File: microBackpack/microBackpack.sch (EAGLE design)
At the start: 71 parts, among them IC1 LM324D, IC2 LM324D, J2 USB_B_PTH, J4 2X6 FEMALE, U1 ATMEGA328P_TQFP, U2 5VREG-HS, U3 CP2102N-QFN24, U4 TVS_DIODE_4PK, U5 MCP4728, U6 78L09F, U7 TVS_DIODE_4PK, U8 TVS_DIODE_4PK, U9 TVS_DIODE_4PK

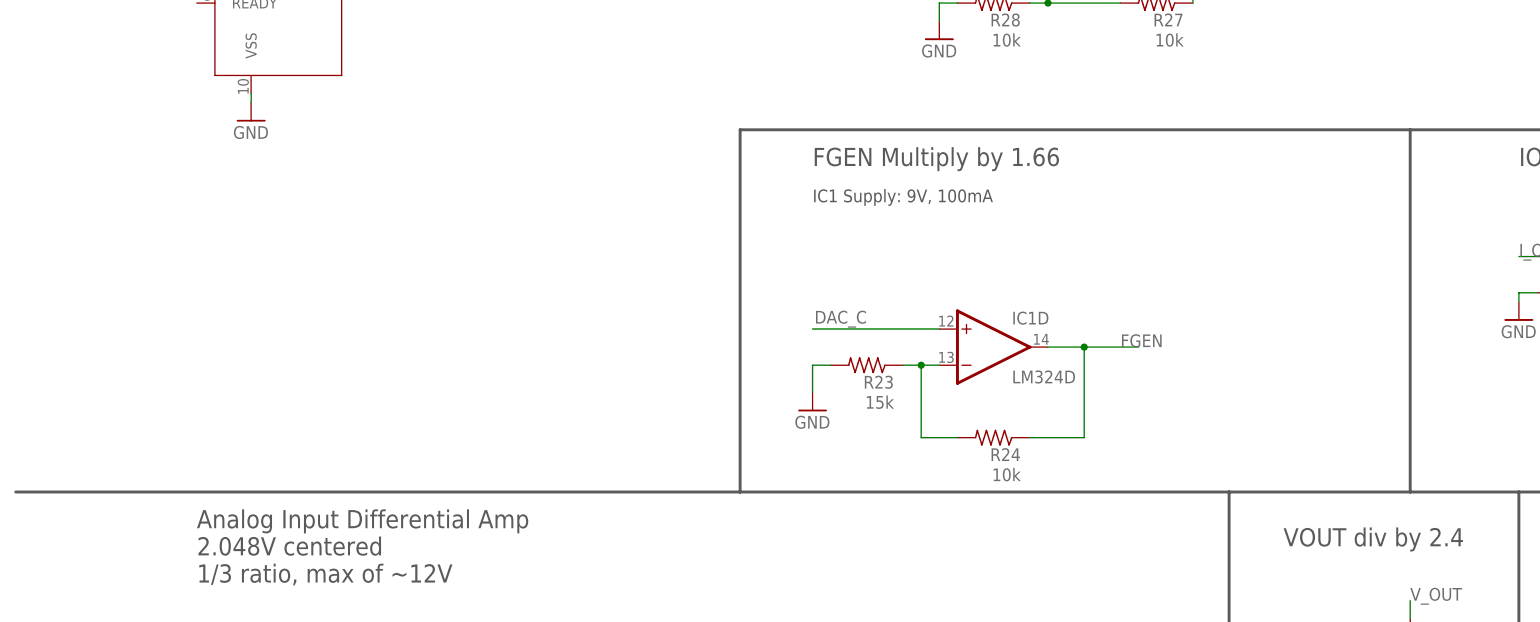
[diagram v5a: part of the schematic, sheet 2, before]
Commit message: Added 2nd order filter to FGEN
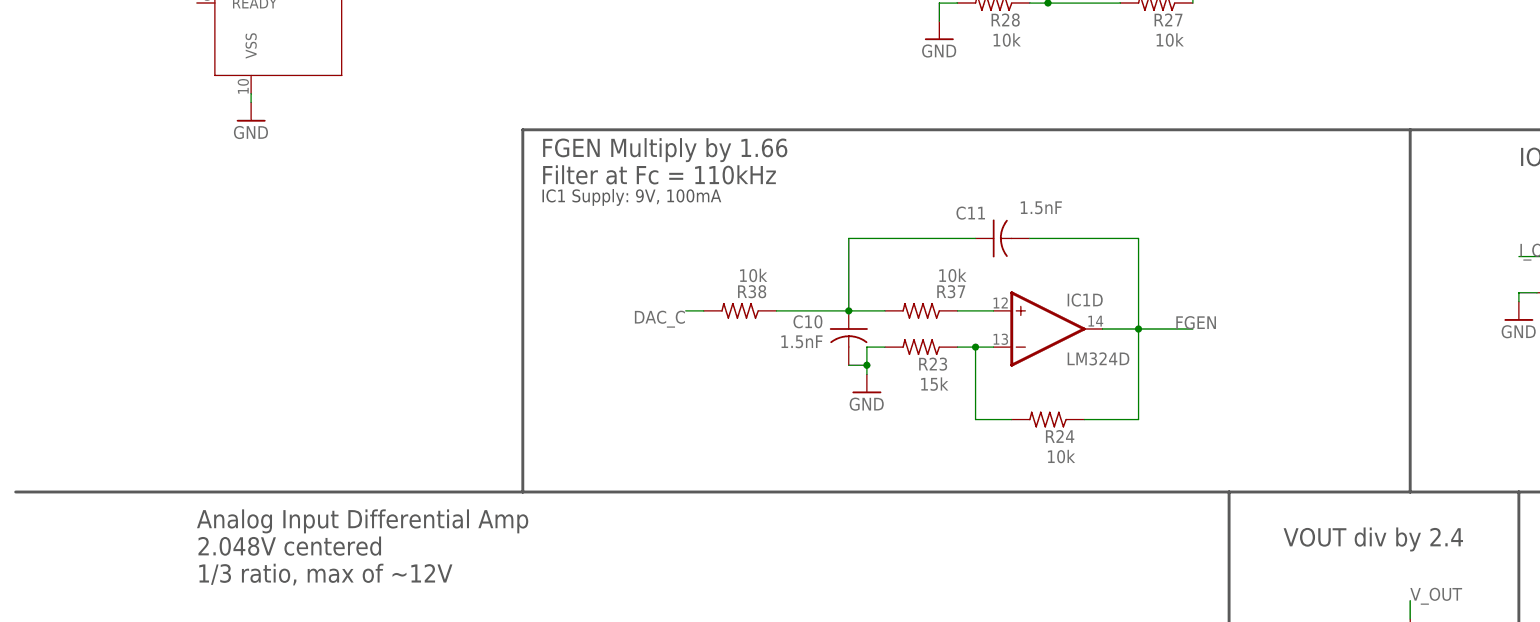
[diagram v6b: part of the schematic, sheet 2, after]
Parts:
- added C10, C11: 1.5nF, rcl:C-USC0805
- added R37, R38: 10k, rcl:R-US_R0805
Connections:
- new net N$12: IC1D.+IN, R37.1
- new net N$4: C10.1, C11.1, R37.2, R38.1
- net DAC_C: now also R38.2; no longer IC1D.+IN
- net FGEN: now also C11.2
- net GND: now also C10.2
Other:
- note added: "FGEN Multiply by 1.66 Filter at Fc = 110kHz"
- note removed: "FGEN Multiply by 1.66"
- moved on the sheet: IC1D, R23, R24
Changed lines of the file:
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@@
 <part name="R35" library="rcl" library_urn="urn:adsk.eagle:library:334" deviceset="R-US_" device="R0805" package3d_urn="urn:adsk.eagle:package:23553/2" value="10"/>
 <part name="R36" library="rcl" library_urn="urn:adsk.eagle:library:334" deviceset="R-US_" device="R0805" package3d_urn="urn:adsk.eagle:package:23553/2" value="10"/>
+<part name="C10" library="rcl" library_urn="urn:adsk.eagle:library:334" deviceset="C-US" device="C0805" package3d_urn="urn:adsk.eagle:package:23617/2" value="1.5nF"/>
+<part name="C11" library="rcl" library_urn="urn:adsk.eagle:library:334" deviceset="C-US" device="C0805" package3d_urn="urn:adsk.eagle:package:23617/2" value="1.5nF"/>
+<part name="R37" library="rcl" library_urn="urn:adsk.eagle:library:334" deviceset="R-US_" device="R0805" package3d_urn="urn:adsk.eagle:package:23553/2" value="10k"/>
+<part name="R38" library="rcl" library_urn="urn:adsk.eagle:library:334" deviceset="R-US_" device="R0805" package3d_urn="urn:adsk.eagle:package:23553/2" value="10k"/>
 </parts>
 <sheets>
@@
 <wire x1="226.06" y1="144.78" x2="271.78" y2="144.78" width="0.4064" layer="97"/>
 <wire x1="177.8" y1="43.18" x2="177.8" y2="93.98" width="0.4064" layer="97"/>
-<wire x1="7.62" y1="93.98" x2="109.22" y2="93.98" width="0.4064" layer="97"/>
-<wire x1="109.22" y1="93.98" x2="177.8" y2="93.98" width="0.4064" layer="97"/>
-<wire x1="203.2" y1="144.78" x2="109.22" y2="144.78" width="0.4064" layer="97"/>
-<wire x1="109.22" y1="144.78" x2="109.22" y2="93.98" width="0.4064" layer="97"/>
-<text x="119.38" y="139.7" size="2.54" layer="97">FGEN Multiply by 1.66</text>
-<text x="119.38" y="134.62" size="1.778" layer="97">IC1 Supply: 9V, 100mA</text>
+<wire x1="7.62" y1="93.98" x2="78.74" y2="93.98" width="0.4064" layer="97"/>
+<wire x1="78.74" y1="93.98" x2="177.8" y2="93.98" width="0.4064" layer="97"/>
+<wire x1="203.2" y1="144.78" x2="78.74" y2="144.78" width="0.4064" layer="97"/>
+<wire x1="78.74" y1="144.78" x2="78.74" y2="93.98" width="0.4064" layer="97"/>
+<text x="81.28" y="137.16" size="2.54" layer="97">FGEN Multiply by 1.66
+Filter at Fc = 110kHz</text>
+<text x="81.28" y="134.62" size="1.778" layer="97">IC1 Supply: 9V, 100mA</text>
 <text x="238.76" y="203.2" size="2.54" layer="97">ISET div by 4</text>
 <wire x1="226.06" y1="144.78" x2="226.06" y2="210.82" width="0.4064" layer="97"/>
@@
 </instance>
 <instance part="IC1" gate="P" x="243.84" y="124.46" smashed="yes"/>
-<instance part="IC1" gate="D" x="144.78" y="114.3" smashed="yes">
-<attribute name="NAME" x="147.32" y="117.475" size="1.778" layer="95"/>
-<attribute name="VALUE" x="147.32" y="109.22" size="1.778" layer="96"/>
+<instance part="IC1" gate="D" x="152.4" y="116.84" smashed="yes">
+<attribute name="NAME" x="154.94" y="120.015" size="1.778" layer="95"/>
+<attribute name="VALUE" x="154.94" y="111.76" size="1.778" layer="96"/>
 </instance>
 <instance part="IC2" gate="A" x="160.02" y="180.34" smashed="yes">
@@
 <attribute name="VALUE" x="162.56" y="175.26" size="1.778" layer="96"/>
 </instance>
-<instance part="R23" gate="G$1" x="127" y="111.76" smashed="yes" rot="R180">
-<attribute name="NAME" x="130.81" y="110.2614" size="1.778" layer="95" rot="R180"/>
-<attribute name="VALUE" x="130.81" y="107.442" size="1.778" layer="96" rot="R180"/>
-</instance>
-<instance part="R24" gate="G$1" x="144.78" y="101.6" smashed="yes" rot="R180">
-<attribute name="NAME" x="148.59" y="100.1014" size="1.778" layer="95" rot="R180"/>
-<attribute name="VALUE" x="148.59" y="97.282" size="1.778" layer="96" rot="R180"/>
-</instance>
-<instance part="GND16" gate="1" x="119.38" y="105.41" smashed="yes">
-<attribute name="VALUE" x="116.84" y="102.87" size="1.778" layer="96"/>
+<instance part="R23" gate="G$1" x="134.62" y="114.3" smashed="yes" rot="R180">
+<attribute name="NAME" x="138.43" y="112.8014" size="1.778" layer="95" rot="R180"/>
+<attribute name="VALUE" x="138.43" y="109.982" size="1.778" layer="96" rot="R180"/>
+</instance>
+<instance part="R24" gate="G$1" x="152.4" y="104.14" smashed="yes" rot="R180">
+<attribute name="NAME" x="156.21" y="102.6414" size="1.778" layer="95" rot="R180"/>
+<attribute name="VALUE" x="156.21" y="99.822" size="1.778" layer="96" rot="R180"/>
+</instance>
+<instance part="GND16" gate="1" x="127" y="107.95" smashed="yes">
+<attribute name="VALUE" x="124.46" y="105.41" size="1.778" layer="96"/>
 </instance>
 <instance part="IC2" gate="P" x="160.02" y="180.34" smashed="yes"/>
@@
 <instance part="GND19" gate="1" x="137.16" y="157.48" smashed="yes">
 <attribute name="VALUE" x="134.62" y="154.94" size="1.778" layer="96"/>
+</instance>
+<instance part="C10" gate="G$1" x="124.46" y="116.84" smashed="yes">
+<attribute name="NAME" x="120.904" y="118.745" size="1.778" layer="95" rot="R180"/>
+<attribute name="VALUE" x="120.904" y="115.951" size="1.778" layer="96" rot="R180"/>
+</instance>
+<instance part="C11" gate="G$1" x="144.78" y="129.54" smashed="yes" rot="R90">
+<attribute name="NAME" x="143.764" y="133.985" size="1.778" layer="95" rot="R180"/>
+<attribute name="VALUE" x="148.336" y="132.969" size="1.778" layer="96"/>
+</instance>
+<instance part="R37" gate="G$1" x="134.62" y="119.38" smashed="yes" rot="R180">
+<attribute name="NAME" x="140.97" y="122.9614" size="1.778" layer="95" rot="R180"/>
+<attribute name="VALUE" x="140.97" y="125.222" size="1.778" layer="96" rot="R180"/>
+</instance>
+<instance part="R38" gate="G$1" x="109.22" y="119.38" smashed="yes" rot="R180">
+<attribute name="NAME" x="113.03" y="122.9614" size="1.778" layer="95" rot="R180"/>
+<attribute name="VALUE" x="113.03" y="125.222" size="1.778" layer="96" rot="R180"/>
 </instance>
 </instances>
@@
 <segment>
 <pinref part="R23" gate="G$1" pin="2"/>
-<wire x1="121.92" y1="111.76" x2="119.38" y2="111.76" width="0.1524" layer="91"/>
+<wire x1="129.54" y1="114.3" x2="127" y2="114.3" width="0.1524" layer="91"/>
 <pinref part="GND16" gate="1" pin="GND"/>
-<wire x1="119.38" y1="111.76" x2="119.38" y2="107.95" width="0.1524" layer="91"/>
+<wire x1="127" y1="114.3" x2="127" y2="111.76" width="0.1524" layer="91"/>
+<wire x1="127" y1="111.76" x2="127" y2="110.49" width="0.1524" layer="91"/>
+<wire x1="127" y1="111.76" x2="124.46" y2="111.76" width="0.1524" layer="91"/>
+<junction x="127" y="111.76"/>
+<pinref part="C10" gate="G$1" pin="2"/>
 </segment>
 <segment>
@@
 </segment>
 <segment>
-<pinref part="IC1" gate="D" pin="+IN"/>
-<wire x1="137.16" y1="116.84" x2="119.38" y2="116.84" width="0.1524" layer="91"/>
-<label x="127" y="119.38" size="1.778" layer="95" rot="R180"/>
+<wire x1="101.6" y1="119.38" x2="104.14" y2="119.38" width="0.1524" layer="91"/>
+<label x="101.6" y="119.38" size="1.778" layer="95" rot="R180"/>
+<pinref part="R38" gate="G$1" pin="2"/>
 </segment>
 </net>
@@
 <pinref part="IC1" gate="D" pin="-IN"/>
 <pinref part="R23" gate="G$1" pin="1"/>
-<wire x1="137.16" y1="111.76" x2="134.62" y2="111.76" width="0.1524" layer="91"/>
-<wire x1="134.62" y1="111.76" x2="132.08" y2="111.76" width="0.1524" layer="91"/>
-<wire x1="134.62" y1="111.76" x2="134.62" y2="101.6" width="0.1524" layer="91"/>
-<junction x="134.62" y="111.76"/>
+<wire x1="144.78" y1="114.3" x2="142.24" y2="114.3" width="0.1524" layer="91"/>
+<wire x1="142.24" y1="114.3" x2="139.7" y2="114.3" width="0.1524" layer="91"/>
+<wire x1="142.24" y1="114.3" x2="142.24" y2="104.14" width="0.1524" layer="91"/>
+<junction x="142.24" y="114.3"/>
 <pinref part="R24" gate="G$1" pin="2"/>
-<wire x1="134.62" y1="101.6" x2="139.7" y2="101.6" width="0.1524" layer="91"/>
+<wire x1="142.24" y1="104.14" x2="147.32" y2="104.14" width="0.1524" layer="91"/>
 </segment>
 </net>
@@
 <segment>
 <pinref part="R24" gate="G$1" pin="1"/>
-<wire x1="149.86" y1="101.6" x2="157.48" y2="101.6" width="0.1524" layer="91"/>
-<wire x1="157.48" y1="101.6" x2="157.48" y2="114.3" width="0.1524" layer="91"/>
+<wire x1="157.48" y1="104.14" x2="165.1" y2="104.14" width="0.1524" layer="91"/>
+<wire x1="165.1" y1="104.14" x2="165.1" y2="116.84" width="0.1524" layer="91"/>
 <pinref part="IC1" gate="D" pin="OUT"/>
-<wire x1="157.48" y1="114.3" x2="152.4" y2="114.3" width="0.1524" layer="91"/>
-<wire x1="157.48" y1="114.3" x2="165.1" y2="114.3" width="0.1524" layer="91"/>
-<junction x="157.48" y="114.3"/>
-<label x="162.56" y="114.3" size="1.778" layer="95"/>
+<wire x1="165.1" y1="116.84" x2="160.02" y2="116.84" width="0.1524" layer="91"/>
+<wire x1="165.1" y1="116.84" x2="172.72" y2="116.84" width="0.1524" layer="91"/>
+<junction x="165.1" y="116.84"/>
+<label x="170.18" y="116.84" size="1.778" layer="95"/>
+<pinref part="C11" gate="G$1" pin="2"/>
+<wire x1="149.86" y1="129.54" x2="165.1" y2="129.54" width="0.1524" layer="91"/>
+<wire x1="165.1" y1="129.54" x2="165.1" y2="116.84" width="0.1524" layer="91"/>
 </segment>
 </net>
@@
 </segment>
 </net>
+<net name="N$4" class="0">
+<segment>
+<pinref part="R37" gate="G$1" pin="2"/>
+<pinref part="C10" gate="G$1" pin="1"/>
+<wire x1="129.54" y1="119.38" x2="124.46" y2="119.38" width="0.1524" layer="91"/>
+<pinref part="R38" gate="G$1" pin="1"/>
+<wire x1="124.46" y1="119.38" x2="114.3" y2="119.38" width="0.1524" layer="91"/>
+<junction x="124.46" y="119.38"/>
+<wire x1="124.46" y1="119.38" x2="124.46" y2="129.54" width="0.1524" layer="91"/>
+<pinref part="C11" gate="G$1" pin="1"/>
+<wire x1="124.46" y1="129.54" x2="142.24" y2="129.54" width="0.1524" layer="91"/>
+</segment>
+</net>
+<net name="N$12" class="0">
+<segment>
+<pinref part="R37" gate="G$1" pin="1"/>
+<pinref part="IC1" gate="D" pin="+IN"/>
+<wire x1="139.7" y1="119.38" x2="144.78" y2="119.38" width="0.1524" layer="91"/>
+</segment>
+</net>

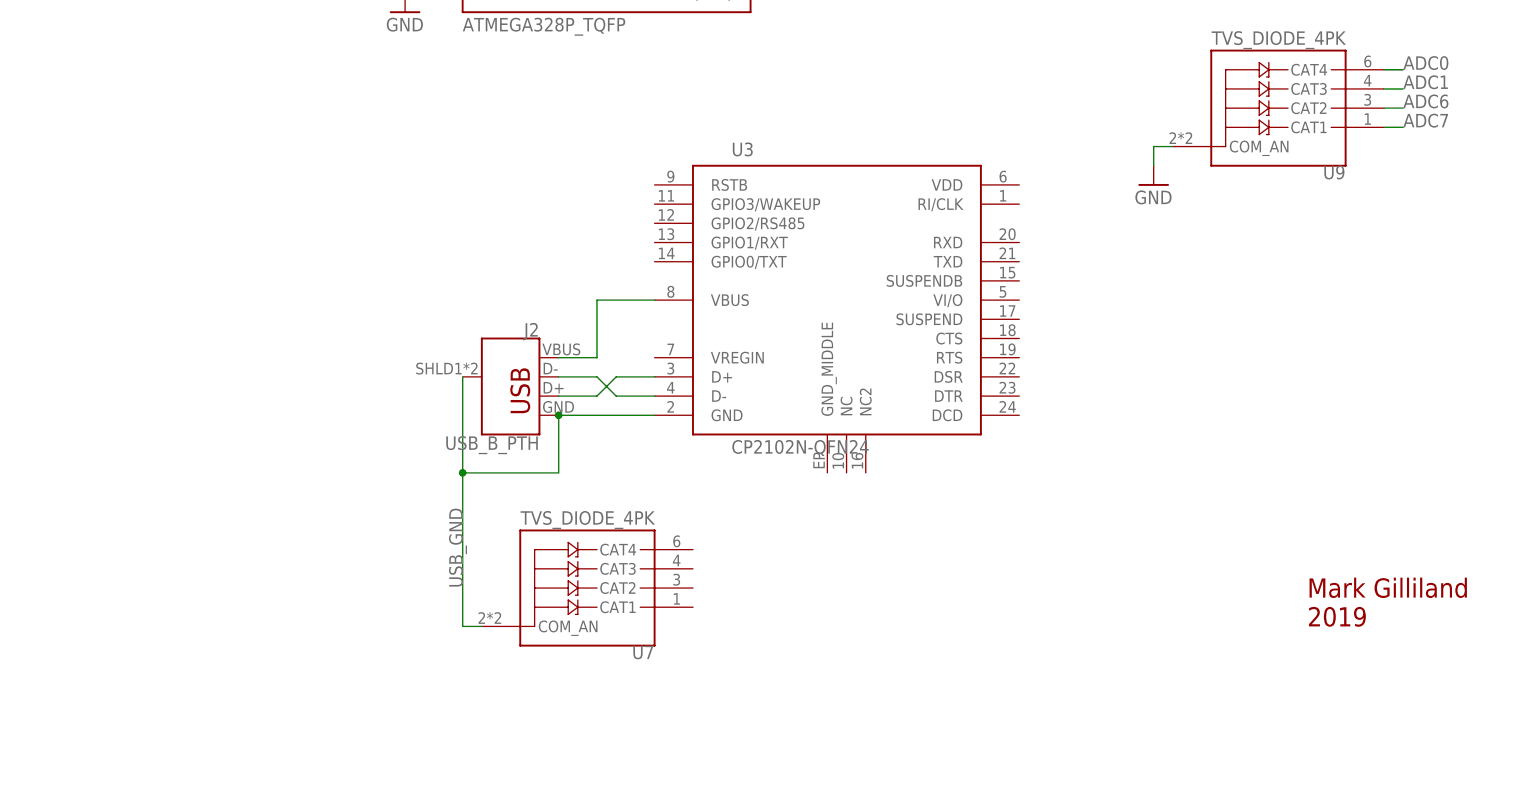
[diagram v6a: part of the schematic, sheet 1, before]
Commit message: Added optoisolators to library. Wired up. Still need to finish USB power circuit.
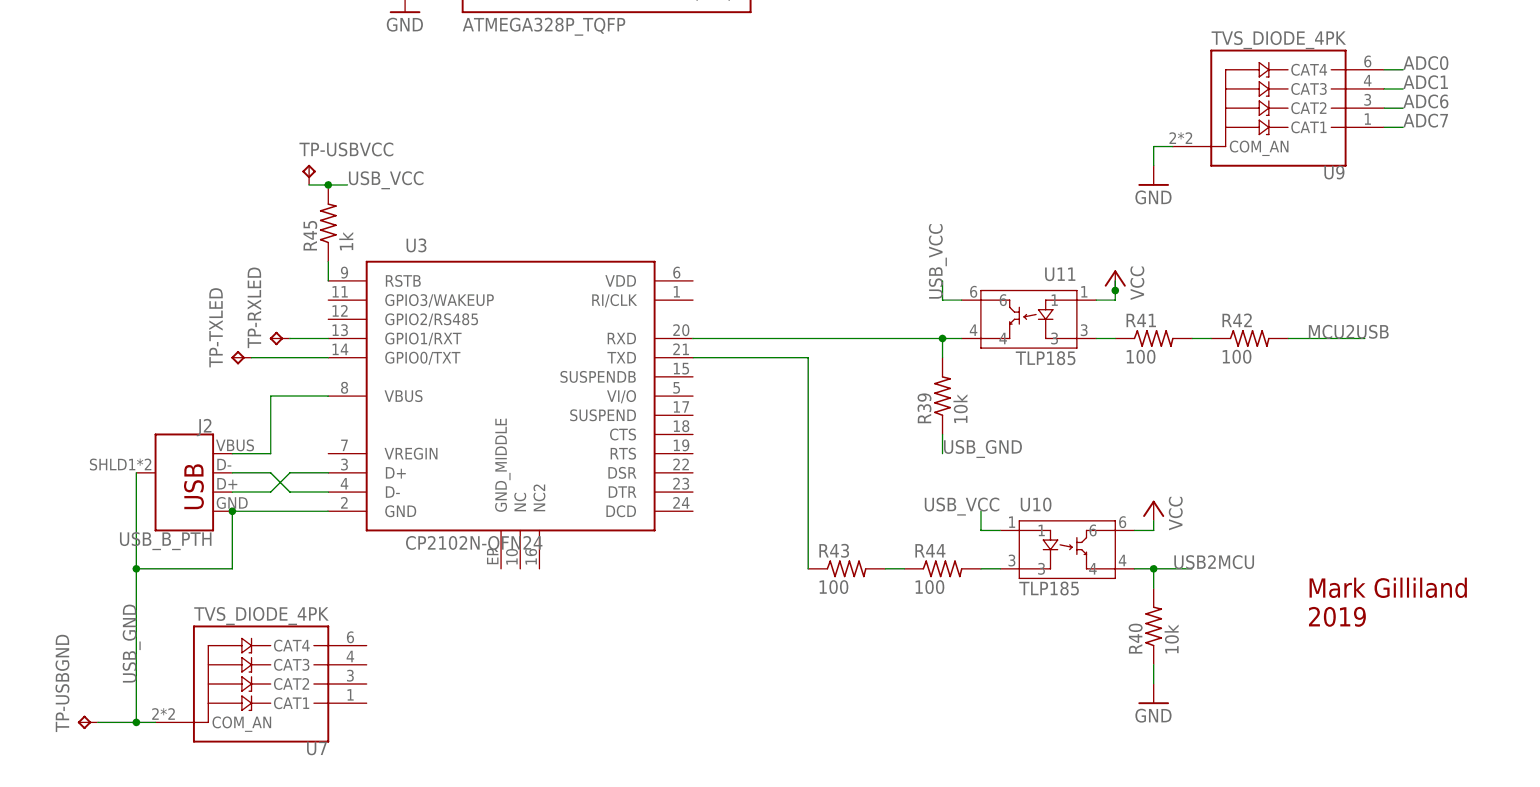
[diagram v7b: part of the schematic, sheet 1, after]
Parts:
- added R39, R40: 10k, rcl:R-US_R0805
- added R41, R42, R43, R44: 100, rcl:R-US_R0603
- added R45: 1k, rcl:R-US_R0805
- added TP-RXLED, TP-TXLED, TP-USBGND, TP-USBVCC: TPPAD1-13, testpad:TPPAD1-13
- added U10, U11: TLP185, microBackpackLib:TLP185
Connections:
- new net N$13: R41.2, R42.1
- new net N$16: R39.2, U11.4, U3.RXD
- new net N$17: R43.2, R44.1
- new net N$18: R44.2, U10.3
- new net N$19: R41.1, U11.3
- new net N$20: R43.1, U3.TXD
- new net N$21: TP-RXLED.TP, U3.GPIO1/RXT
- new net N$22: TP-TXLED.TP, U3.GPIO0/TXT
- new net N$23: R45.1, U3.RSTB
- new net USB_VCC: R45.2, TP-USBVCC.TP, U10.1, U11.6
- net GND: now also R40.1
- net MCU2USB: now also R42.2
- net USB2MCU: now also R40.2, U10.4
- net USB_GND: now also R39.1, TP-USBGND.TP
- net VCC: now also U10.6, U11.1
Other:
- moved on the sheet: J2, U3, U7
